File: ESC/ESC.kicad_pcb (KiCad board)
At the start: 4 copper layers, 80 x 55 mm, 141 parts, among them IC1 TCAN3403DDFRQ1, IC2 UCC27211DR, IC3 UCC27211DR, IC4 UCC27211DR, IC5 STM32G473CCT3, IC6 BD433M5FP-CE2, J1 JST PH 4Pin, J2 JST SH 5Pin, J3 JST SH 3Pin, J4 MR30PW-M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

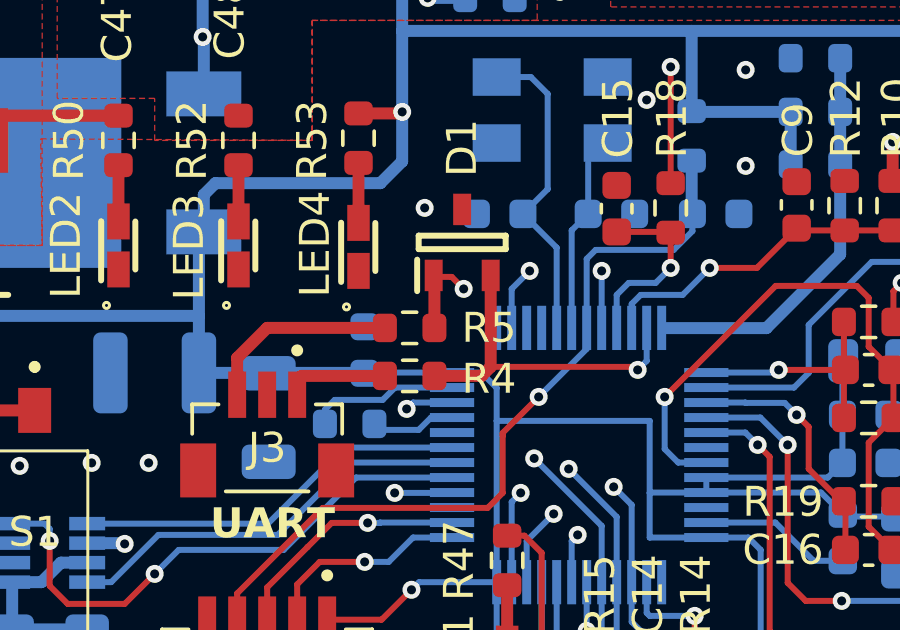
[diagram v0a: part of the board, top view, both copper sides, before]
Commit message: Components library added
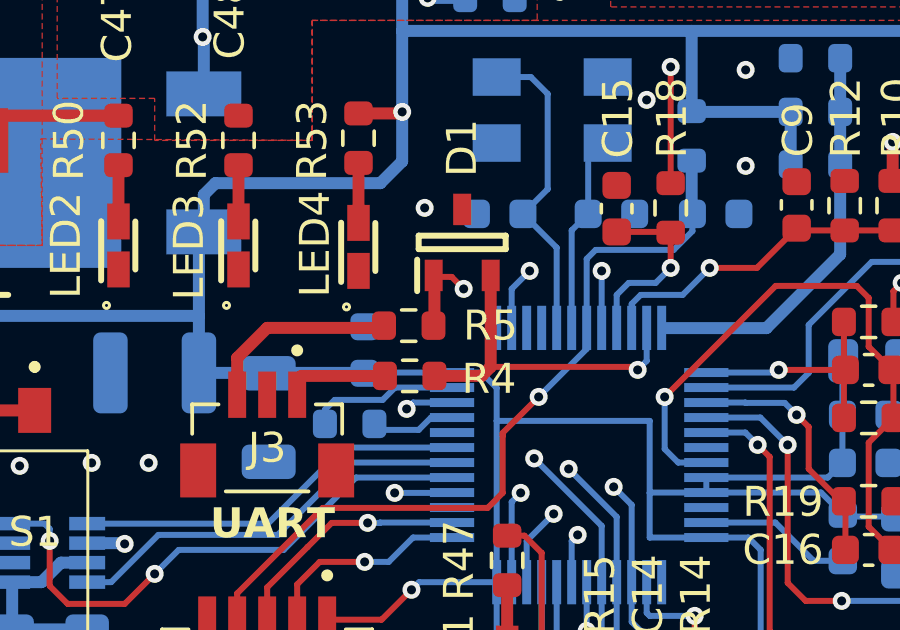
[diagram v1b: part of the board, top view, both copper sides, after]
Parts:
- moved R5 0.08 mm to (136.9, 100.0)
